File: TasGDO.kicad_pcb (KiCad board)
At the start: 4 copper layers, 22 x 22.2 mm, 37 parts, among them J1 Conn_01x04, J10 USB_C_Receptacle_USB2.0_16P, J3 Conn_01x03, K1 AQY212GSX, SW1 SW_Push, SW2 KSC241J LFS, U2 Conv_AMS1117S-3.3, U3 ESP32-C3, Y2 ECS-400-10-37B2-CKM-TR

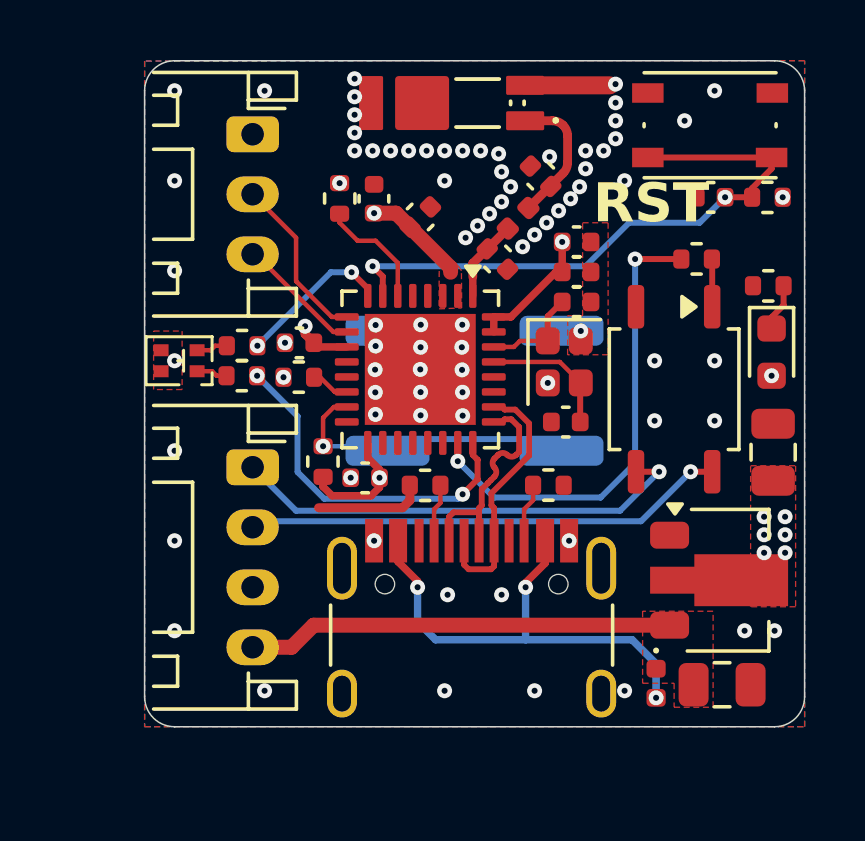
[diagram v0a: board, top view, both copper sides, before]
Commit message: fix: relay pin placement
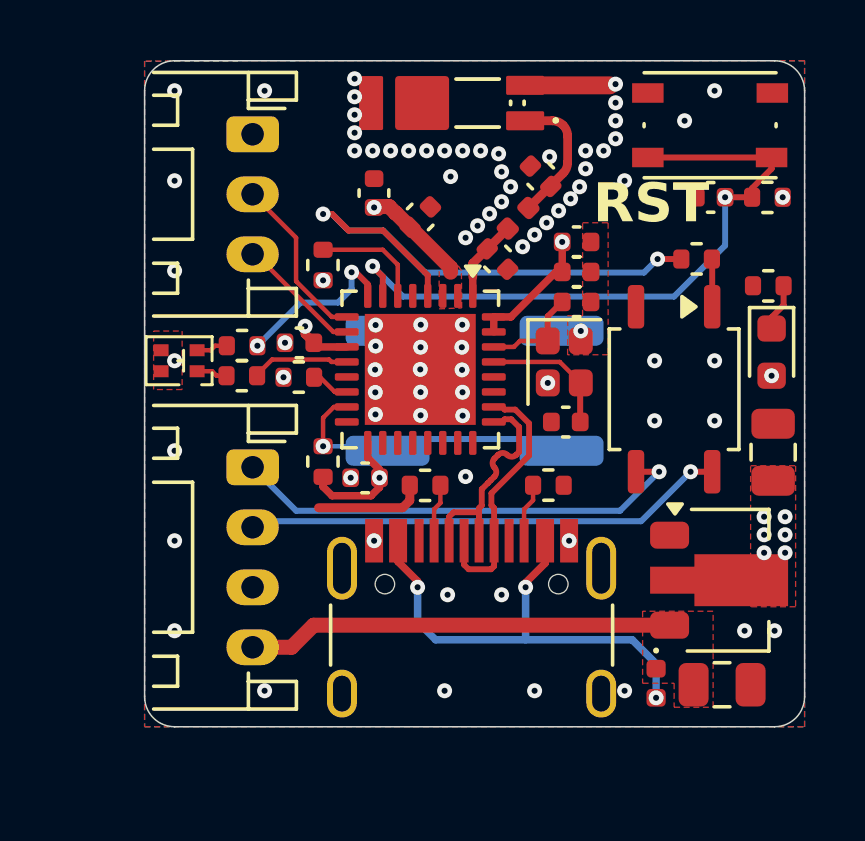
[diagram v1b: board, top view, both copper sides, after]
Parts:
- moved R3 2.29 mm to (139.3, 67.0), turned to 90 degrees
- moved C4 0.19 mm to (141.1, 64.6)
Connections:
- U3 pad 12: unconnected-(U3-MTCK-Pad12) -> /RELAY_LED
- U3 pad 23: /RELAY -> unconnected-(U3-SPID-Pad23)
- U3 pad 24: /RELAY_LED -> unconnected-(U3-SPIQ-Pad24)
- U3 pad 4: unconnected-(U3-XTAL_32K_P-Pad4) -> /RELAY
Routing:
- net /RELAY_LED: track 11.7 -> 3.27 mm, vias 2 -> 0
- net /RELAY: track 15.9 -> 18.0 mm
- net /EN: track 20.5 -> 22.2 mm
- net GND: vias 78 -> 79

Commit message: feat: minor updates
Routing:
- net +3.3V: track 13.9 -> 13.2 mm

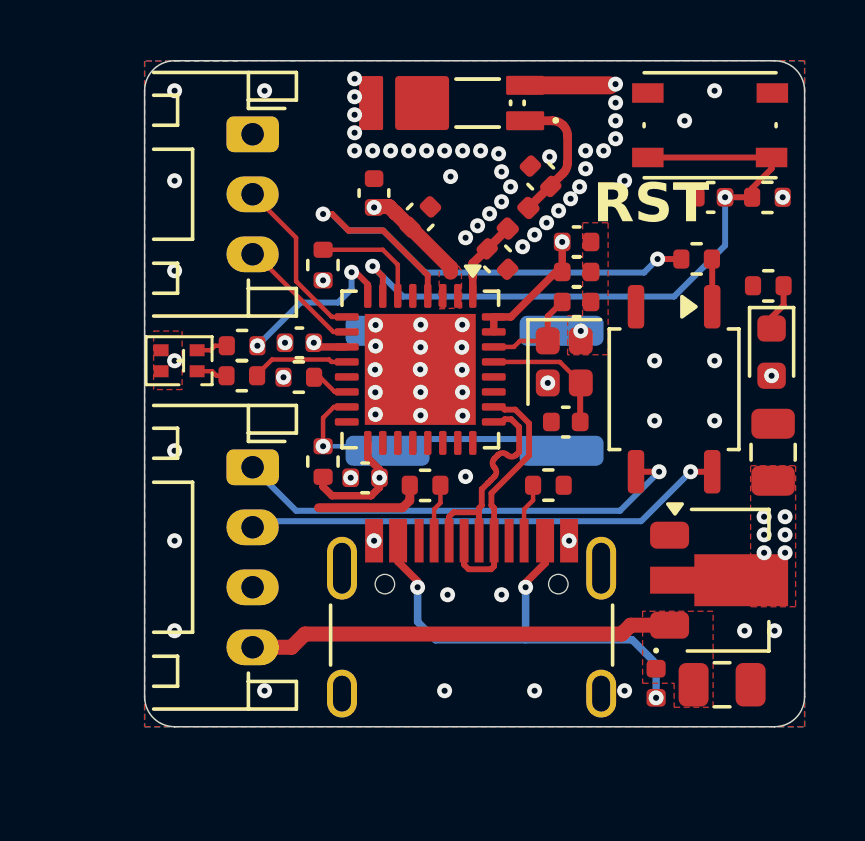
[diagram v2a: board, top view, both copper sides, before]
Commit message: fix: switch to switching power supply
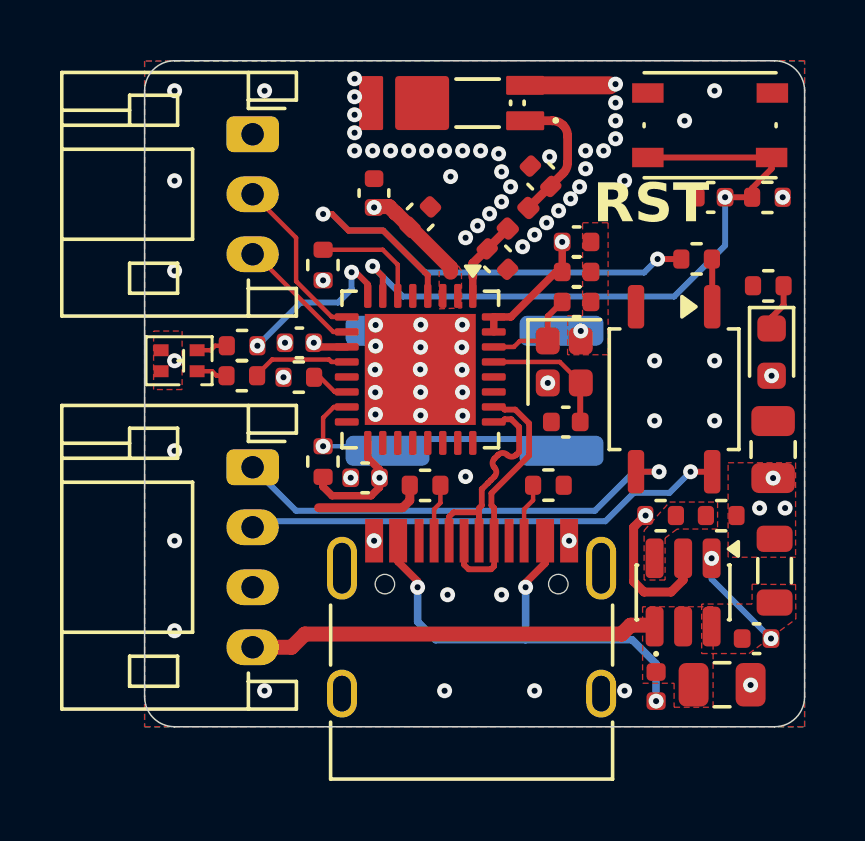
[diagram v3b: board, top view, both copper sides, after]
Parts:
- removed U2: Conv_AMS1117S-3.3, Hardware Components:SOT-89-3
- added C5: 100n, Hardware Components:C_0402_1005Metric, F.Cu at (153.8, 79.4)
- added L2: 10u, Hardware Components:L_0805_2012Metric, F.Cu at (154.4, 77.1)
- added R10: 69k8, Hardware Components:R_0402_1005Metric, F.Cu at (152.6, 75.3)
- added R9: 22k1, Hardware Components:R_0402_1005Metric, F.Cu at (150.6, 75.3)
- added U1: Conv_LMR54410DBVR, Hardware Components:SOT-23-6, F.Cu at (151.3, 77.9)
- C9: value 10u -> 22u
- moved D1 0.11 mm to (150.4, 81.0)
- moved C9 0.09 mm to (154.3, 73.1)
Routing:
- net GND: track 6.47 -> 11.5 mm
- net Net-(U1-CB): track 0.00 -> 3.50 mm, vias 0 -> 2
- net +3.3V: vias 14 -> 11
- added copper zone on F.Cu, net Net-(U1-FB)
- added copper zone on F.Cu, net Net-(U1-SW)
